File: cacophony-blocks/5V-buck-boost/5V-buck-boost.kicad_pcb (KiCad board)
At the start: 4 copper layers, 17 parts, among them U1 TPS63070

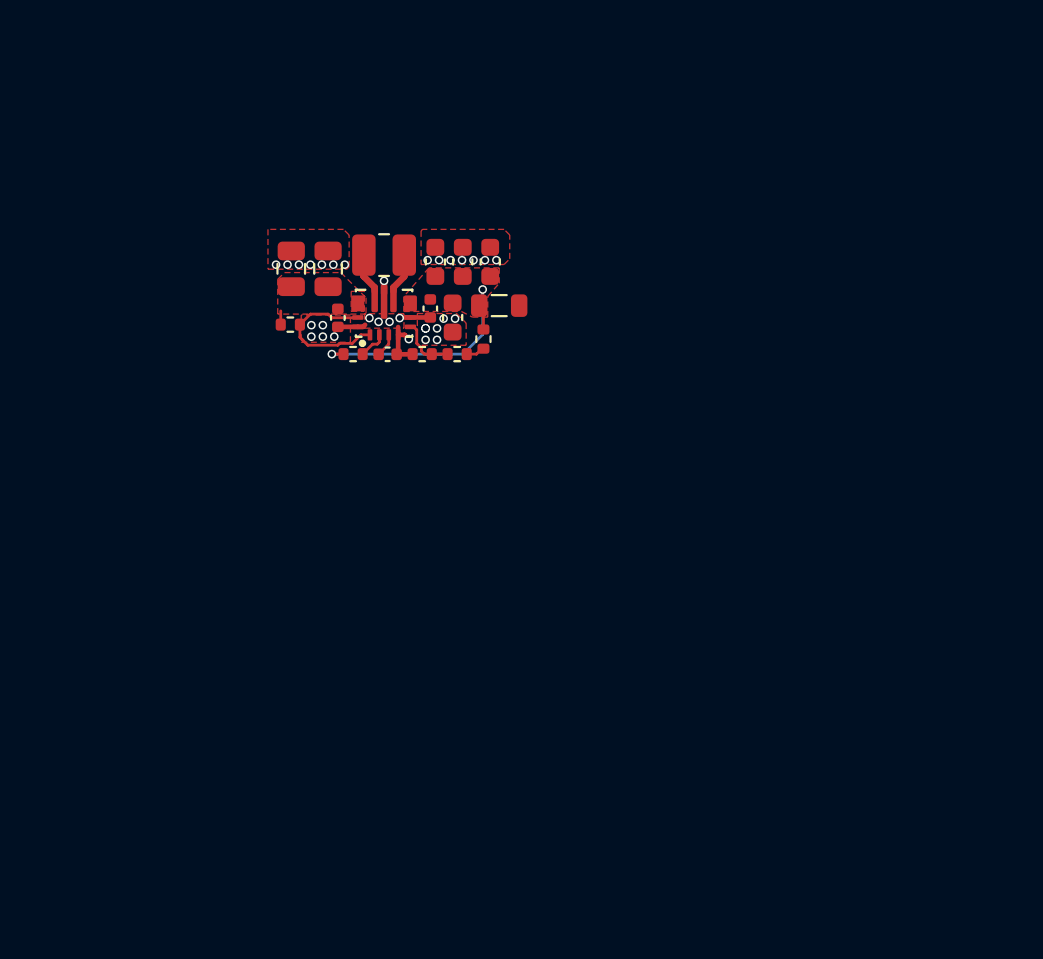
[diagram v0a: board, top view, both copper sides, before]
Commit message: Added 5V design block
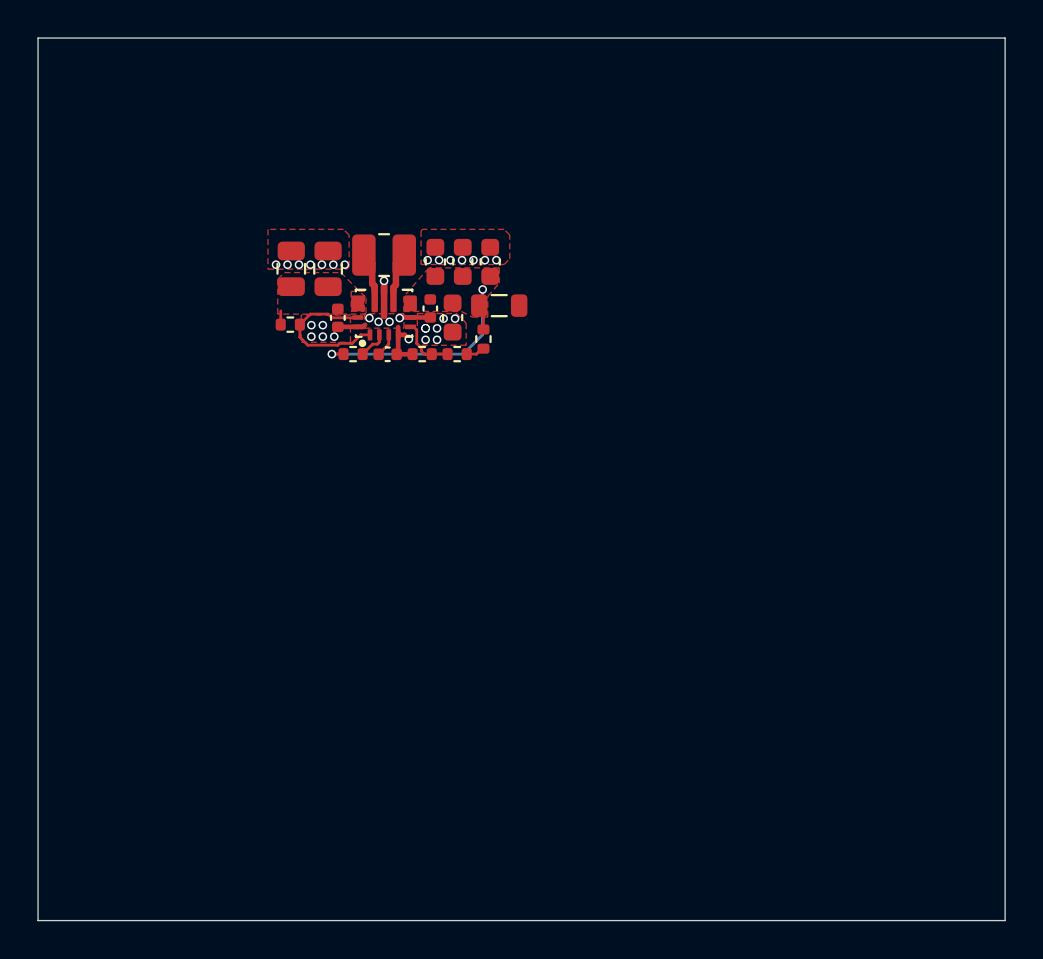
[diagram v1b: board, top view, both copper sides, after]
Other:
- board outline added: 51.5 x 47 mm

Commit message: Update library for solar-tester
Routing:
- net GND: track 6.58 -> 6.44 mm, vias 32 -> 30
- added copper zone on B.Cu, net GND
- added copper zone on In1.Cu, net GND
- added copper zone on In2.Cu, net GND
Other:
- board size 51.5 x 47 mm -> 21 x 14 mm
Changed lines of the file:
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@@
 		(capping no)
 		(filling no)
+		(zone_defaults)
 		(pcbplotparams
 			(layerselection 0x00000000_00000000_55555555_5755f5ff)
@@
 	)
 	(gr_rect
-		(start -18.42 -14.65)
-		(end 33.06 32.33)
+		(start -10 -8)
+		(end 11 6)
 		(stroke
 			(width 0.05)
@@
 	)
 	(segment
-		(start 1.095 1.15)
-		(end 0.75 1.15)
+		(start 1.2225 1.2775)
+		(end 1.095 1.15)
 		(width 0.25)
 		(layer "F.Cu")
@@
 	)
 	(segment
-		(start 1.32 1.375)
-		(end 1.095 1.15)
+		(start 1.095 1.15)
+		(end 0.75 1.15)
 		(width 0.25)
 		(layer "F.Cu")
@@
 	)
 	(via
-		(at 1.32 1.375)
+		(at 1.2225 1.2775)
 		(size 0.46)
 		(drill 0.3)
@@
 	)
 	(via
-		(at -3.87 0.635)
+		(at -3.76 0.595)
 		(size 0.46)
 		(drill 0.3)
@@
 	)
 	(via
-		(at 0.83 0.255)
+		(at 0.64 0.37)
 		(size 0.46)
 		(drill 0.3)
@@
 	)
 	(via
-		(at -3.26 0.635)
+		(at -3.15 0.595)
 		(size 0.46)
 		(drill 0.3)
@@
 	)
 	(via
-		(at -0.29 0.455)
-		(size 0.46)
-		(drill 0.3)
-		(layers "F.Cu" "B.Cu")
-		(free yes)
-		(net "GND")
-	)
-	(via
-		(at 2.21 0.805)
+		(at -0.64 0.37)
 		(size 0.46)
 		(drill 0.3)
@@
 	)
 	(via
-		(at -0.78 0.255)
-		(size 0.46)
-		(drill 0.3)
-		(layers "F.Cu" "B.Cu")
-		(free yes)
-		(net "GND")
-	)
-	(via
-		(at 0.29 0.455)
+		(at 0 0.505)
 		(size 0.46)
 		(drill 0.3)
@@
 	)
 	(zone
+		(net "GND")
+		(layers "F.Cu" "B.Cu" "In1.Cu" "In2.Cu")
+		(hatch edge 0.5)
+		(connect_pads
+			(clearance 0.5)
+		)
+		(min_thickness 0.25)
+		(fill yes
+			(thermal_gap 0.5)
+			(thermal_bridge_width 0.5)
+			(island_removal_mode 0)
+		)
+		(polygon
+			(pts
+				(xy -9 -7) (xy 10 -7) (xy 10 5) (xy -9 5)
+			)
+		)
+	)
+	(zone
 		(layers "F.Cu" "In1.Cu")
 		(hatch edge 0.5)
@@
 			(tracks allowed)
 			(vias not_allowed)
-			(pads not_allowed)
+			(pads allowed)
 			(copperpour not_allowed)
 			(footprints allowed)
@@
 			"17c92423-7983-46b7-8a62-efea801a8a67" "189341f0-9e6c-49a2-8f47-9ebcfa1dda39"
 			"18f006ee-1bc5-4da5-8b1f-faa0336a5c2e" "195b5aa4-7657-4fe0-854d-4a6e1311fe3b"
-			"1a421abc-7c26-4017-80a9-2e38798bd0d1" "1b5dc17c-5c3b-48ea-8e44-4ea4ed7604d8"
-			"1dbfe832-5248-4b07-96b4-05302e3d4f15" "1e91a866-51bd-4dc0-89b5-5974c37557e5"
-			"20ba0754-7097-4f6d-9250-c4da089e6918" "225e00fc-68d0-4829-94de-dc975e84c770"
-			"246d923a-0abe-4545-885c-ffd99e981cc8" "24926ddf-18c4-411e-b18f-c628b4402a2b"
-			"266aee12-646b-4acf-9d04-51a9b9f45192" "2673d264-42af-4d02-8b2a-581da257e055"
-			"2c082948-9adc-49bf-a248-cf80ac6845be" "2e7b5796-2300-4f0e-894b-deb4be7ea1b7"
-			"3263dd0f-b2c4-46ce-86d0-a99ecb8600cd" "34f443dd-9a94-4b06-a8c0-d103f3e0d18f"
-			"37d1fc60-7c7e-4408-8e6d-ac96c02a39b5" "383a3590-6c71-4d66-9fa4-2c2a68efbf78"
-			"38ad897b-8158-4784-98f6-ec1d34ae1249" "3ae15677-db4b-4354-b099-c6917e0ff41f"
+			"1a421abc-7c26-4017-80a9-2e38798bd0d1" "1dbfe832-5248-4b07-96b4-05302e3d4f15"
+			"1e91a866-51bd-4dc0-89b5-5974c37557e5" "20ba0754-7097-4f6d-9250-c4da089e6918"
+			"225e00fc-68d0-4829-94de-dc975e84c770" "246d923a-0abe-4545-885c-ffd99e981cc8"
+			"24926ddf-18c4-411e-b18f-c628b4402a2b" "266aee12-646b-4acf-9d04-51a9b9f45192"
+			"2673d264-42af-4d02-8b2a-581da257e055" "2c082948-9adc-49bf-a248-cf80ac6845be"
+			"2e7b5796-2300-4f0e-894b-deb4be7ea1b7" "3263dd0f-b2c4-46ce-86d0-a99ecb8600cd"
+			"34f443dd-9a94-4b06-a8c0-d103f3e0d18f" "37d1fc60-7c7e-4408-8e6d-ac96c02a39b5"
+			"383a3590-6c71-4d66-9fa4-2c2a68efbf78" "38ad897b-8158-4784-98f6-ec1d34ae1249"
+			"38c0bc60-a9a2-472c-9238-5cc7896ca150" "3ae15677-db4b-4354-b099-c6917e0ff41f"
 			"3c09eaba-97b7-478a-a129-73a60f554a86" "3d6f975c-a2ec-4252-aece-d9ed5866144b"
 			"3dea0c43-72ae-446e-947a-092a124fe01b" "3e67290c-70a0-4f72-b7ef-8af030397e14"
@@
 			"ad041e6e-ed15-4fec-9e09-ad51c0db1ccb" "aec6b133-b1f0-40b7-b3d5-65cbcf731fd9"
 			"af7cdb57-3a09-48b6-88ec-8613f71af0f8" "b660282e-9f9d-4144-9ed6-f4e81eb08452"
-			"b69d9f32-390a-4b00-9e84-fd6ce835bcde" "b99442e0-bab0-4137-8855-fd8a17e6abc3"
-			"bcad13c6-3cb1-4b96-92a6-b02c0bb0f46b" "bdcd1c3b-bec9-4b07-8aa7-4587c6a90808"
-			"bdda020d-7e6e-4186-8e1b-c2e69b012c0e" "c27b2bd0-93e3-4242-8dc1-dd9b42c64b4e"
-			"c3866772-05ec-4f80-b260-538d3c51732a" "ca1e0f74-4c8a-4504-a45a-a07eea5a6c3e"
+			"b69d9f32-390a-4b00-9e84-fd6ce835bcde" "bdcd1c3b-bec9-4b07-8aa7-4587c6a90808"
+			"bdda020d-7e6e-4186-8e1b-c2e69b012c0e" "be37032c-9146-4865-baed-96cf415d14c8"
+			"c27b2bd0-93e3-4242-8dc1-dd9b42c64b4e" "ca1e0f74-4c8a-4504-a45a-a07eea5a6c3e"
 			"ccdc9b03-618b-4da9-819d-0f49d059ca2d" "d3f3b40c-a485-4223-9f79-033a214a8968"
 			"d409b750-9253-4f1e-a211-fded902c7a9a" "d60215fb-e507-4bbc-bb29-f2f72948d219"
